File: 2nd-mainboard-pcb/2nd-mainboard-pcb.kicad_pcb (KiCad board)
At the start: 2 copper layers, 1 part, among them P1 USB_C_Plug_USB2.0

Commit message: managed libraries
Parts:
- added SW1: SW_DIP_x01, Button_Switch_SMD:SW_SPST_EVQQ2, F.Cu at (196.2, 59.4)
- added U1: ATmega328PB-A, Package_QFP:TQFP-32_7x7mm_P0.8mm, F.Cu at (131.1, 52.8)
- added U2: FT232RL, Package_SO:SSOP-28_5.3x10.2mm_P0.65mm, F.Cu at (120.0, 53.0)

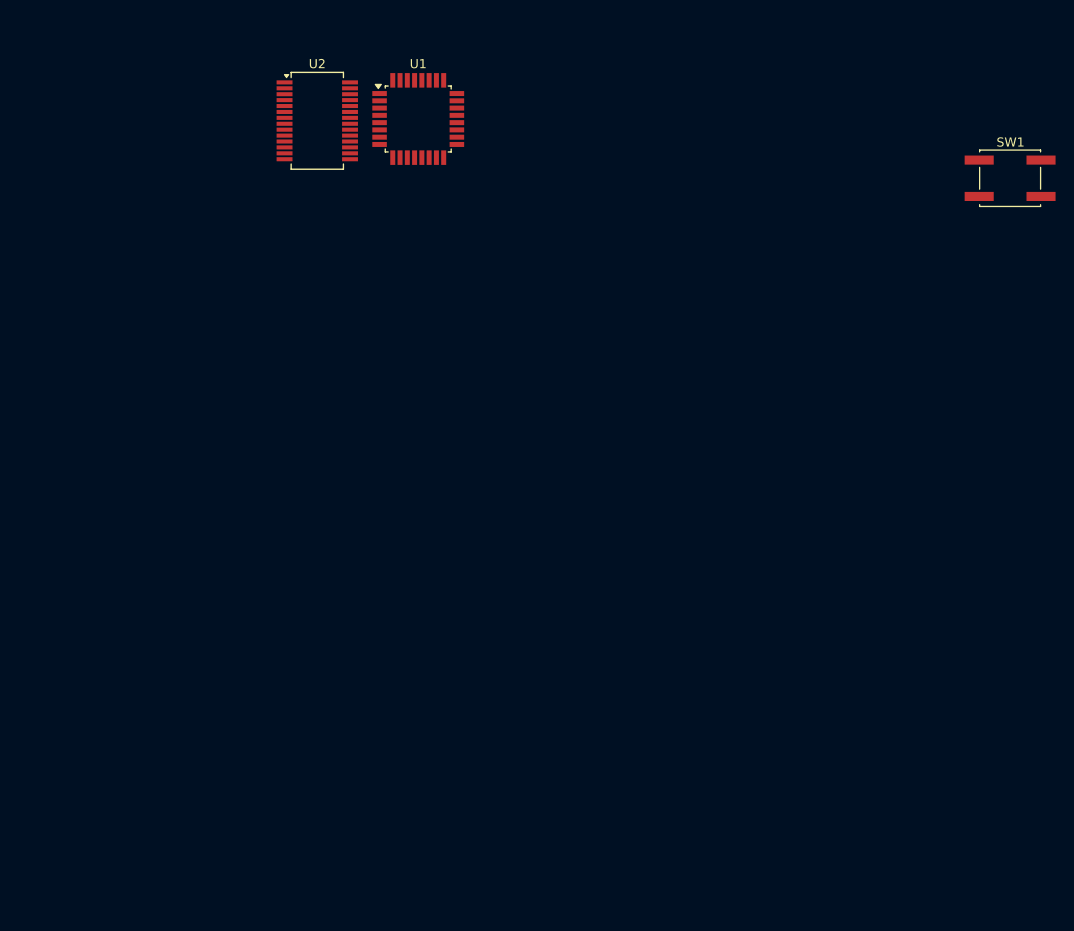
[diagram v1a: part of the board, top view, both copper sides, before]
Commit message: added test point and documentation
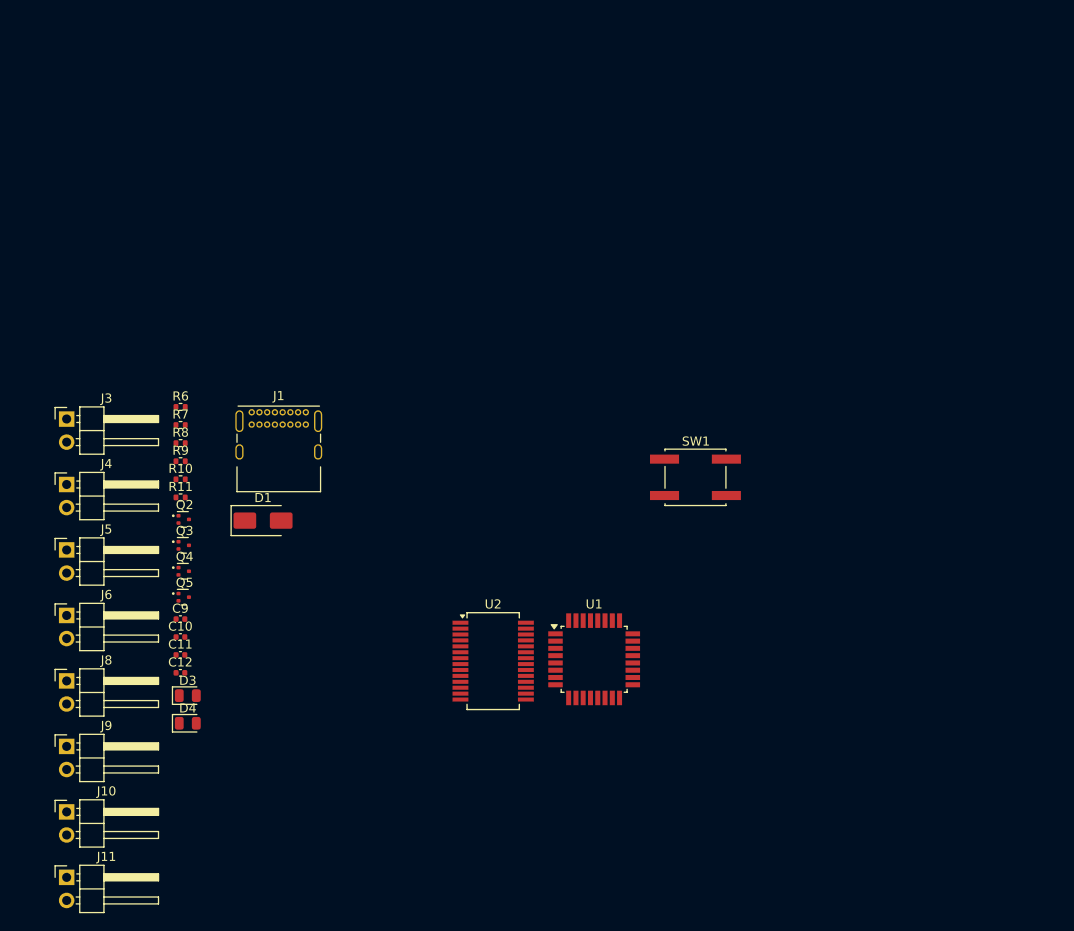
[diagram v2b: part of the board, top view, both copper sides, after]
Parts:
- added C10: 0.1µF, Capacitor_SMD:C_0402_1005Metric, F.Cu at (105.0, 109.8)
- added C11: 0.1µF, Capacitor_SMD:C_0402_1005Metric, F.Cu at (105.0, 111.8)
- added C12: 0.1µF, Capacitor_SMD:C_0402_1005Metric, F.Cu at (105.0, 113.8)
- added C9: 0.1µF, Capacitor_SMD:C_0402_1005Metric, F.Cu at (105.0, 107.8)
- added D1: SMAJ5.0A, Diode_SMD:D_SMA, F.Cu at (114.0, 97.0)
- added D3: YELLOW, LED_SMD:LED_0805_2012Metric, F.Cu at (105.8, 116.3)
- added D4: YELLOW, LED_SMD:LED_0805_2012Metric, F.Cu at (105.8, 119.3)
- added J1: USB_C_Receptacle, Connector_USB:USB_C_Receptacle_GCT_USB4085, F.Cu at (112.8, 85.1)
- added J10: FAN2, Connector_PinHeader_2.54mm:PinHeader_1x02_P2.54mm_Horizontal, F.Cu at (92.4, 129.0)
- added J11: FAN4, Connector_PinHeader_2.54mm:PinHeader_1x02_P2.54mm_Horizontal, F.Cu at (92.4, 136.2)
- added J3: T0, Connector_PinHeader_2.54mm:PinHeader_1x02_P2.54mm_Horizontal, F.Cu at (92.4, 85.8)
- added J4: T1, Connector_PinHeader_2.54mm:PinHeader_1x02_P2.54mm_Horizontal, F.Cu at (92.4, 93.0)
- added J5: T2, Connector_PinHeader_2.54mm:PinHeader_1x02_P2.54mm_Horizontal, F.Cu at (92.4, 100.2)
- added J6: T3, Connector_PinHeader_2.54mm:PinHeader_1x02_P2.54mm_Horizontal, F.Cu at (92.4, 107.4)
- added J8: FAN0, Connector_PinHeader_2.54mm:PinHeader_1x02_P2.54mm_Horizontal, F.Cu at (92.4, 114.6)
- added J9: FAN1, Connector_PinHeader_2.54mm:PinHeader_1x02_P2.54mm_Horizontal, F.Cu at (92.4, 121.8)
- added Q2: DTC143E, Package_TO_SOT_SMD:SOT-723, F.Cu at (105.3, 96.9)
- added Q3: DTC143E, Package_TO_SOT_SMD:SOT-723, F.Cu at (105.3, 99.7)
- added Q4: DTC143E, Package_TO_SOT_SMD:SOT-723, F.Cu at (105.3, 102.6)
- added Q5: DTC143E, Package_TO_SOT_SMD:SOT-723, F.Cu at (105.3, 105.4)
- added R10: 4k7, Resistor_SMD:R_0402_1005Metric, F.Cu at (105.0, 92.5)
- added R11: 330, Resistor_SMD:R_0402_1005Metric, F.Cu at (105.0, 94.5)
- added R6: 4k7, Resistor_SMD:R_0402_1005Metric, F.Cu at (105.0, 84.5)
- added R7: 4k7, Resistor_SMD:R_0402_1005Metric, F.Cu at (105.0, 86.5)
- added R8: 330, Resistor_SMD:R_0402_1005Metric, F.Cu at (105.0, 88.5)
- added R9: 4k7, Resistor_SMD:R_0402_1005Metric, F.Cu at (105.0, 90.5)
- moved U1 62.5 mm to (150.5, 112.3)
- moved U2 62.5 mm to (139.4, 112.5)
- moved SW1 47.7 mm to (161.6, 92.3)
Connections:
- SW1 pad 1: unconnected-(SW1-Pad1) -> GND
- SW1 pad 2: unconnected-(SW1-Pad2) -> reset
- U1 pad 12: unconnected-(U1-PB0-Pad12) -> FAN_0_PWM
- U1 pad 13: unconnected-(U1-PB1-Pad13) -> FAN_1_PWM
- U1 pad 14: unconnected-(U1-PB2-Pad14) -> FAN_2_PWM
- U1 pad 15: unconnected-(U1-PB3-Pad15) -> FAN_3_PWM
- U1 pad 16: unconnected-(U1-PB4-Pad16) -> LED_0
- U1 pad 17: unconnected-(U1-PB5-Pad17) -> LED_1
- U1 pad 18: unconnected-(U1-AVCC-Pad18) -> AREF
- U1 pad 20: unconnected-(U1-AREF-Pad20) -> AREF
- U1 pad 23: unconnected-(U1-PC0-Pad23) -> ADC0
- U1 pad 24: unconnected-(U1-PC1-Pad24) -> ADC1
- U1 pad 25: unconnected-(U1-PC2-Pad25) -> ADC2
- U1 pad 26: unconnected-(U1-PC3-Pad26) -> ADC3
- U1 pad 29: unconnected-(U1-~{RESET}/PC6-Pad29) -> reset
- U1 pad 30: unconnected-(U1-PD0-Pad30) -> RXD
- U1 pad 31: unconnected-(U1-PD1-Pad31) -> TXD
- U1 pad 4: +5V -> AREF
- U1 pad 7: unconnected-(U1-XTAL1/PB6-Pad7) -> Net-(U1-XTAL1/PB6)
- U1 pad 8: unconnected-(U1-XTAL2/PB7-Pad8) -> Net-(U1-XTAL2/PB7)
- U2 pad 1: unconnected-(U2-TXD-Pad1) -> TXD
- U2 pad 15: unconnected-(U2-USBD+-Pad15) -> USBD+
- U2 pad 16: unconnected-(U2-USBD--Pad16) -> USBD-
- U2 pad 19: unconnected-(U2-~{RESET}-Pad19) -> reset
- U2 pad 20: +5V -> AREF
- U2 pad 22: unconnected-(U2-CBUS1-Pad22) -> Net-(U2-CBUS1)
- U2 pad 23: unconnected-(U2-CBUS0-Pad23) -> Net-(U2-CBUS0)
- U2 pad 4: unconnected-(U2-VCCIO-Pad4) -> AREF
- U2 pad 5: unconnected-(U2-RXD-Pad5) -> RXD

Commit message: jtag funktionalität
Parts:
- removed P1: USB_C_Plug_USB2.0, Connector_USB:USB_C_Receptacle_GCT_USB4085
- added A1: Pololu_Breakout_DRV8825, Module:Pololu_Breakout-16_15.2x20.3mm, F.Cu at (218.7, 56.1)
- added C13: 0.1µF, Capacitor_SMD:CP_Elec_5x3, F.Cu at (187.9, 122.1)
- added C14: 0.22µF, Capacitor_SMD:C_0402_1005Metric, F.Cu at (184.9, 126.5)
- added C15: 0.22µF, Capacitor_SMD:C_0402_1005Metric, F.Cu at (184.9, 128.5)
- added C16: 0.1µF, Capacitor_SMD:C_0402_1005Metric, F.Cu at (184.9, 130.5)
- added C17: 0.1µF, Capacitor_SMD:C_0402_1005Metric, F.Cu at (184.9, 132.4)
- added C8: 0.1µF, Capacitor_SMD:CP_Elec_5x3, F.Cu at (187.9, 115.3)
- added D5: YELLOW, LED_SMD:LED_0805_2012Metric, F.Cu at (185.7, 137.0)
- added D6: YELLOW, LED_SMD:LED_0805_2012Metric, F.Cu at (185.7, 140.0)
- added D7: GREEN, LED_SMD:LED_0805_2012Metric, F.Cu at (257.3, 116.4)
- added J12: Fan_12/5V_Regelung, Connector_PinHeader_2.54mm:PinHeader_1x03_P2.54mm_Horizontal, F.Cu at (208.1, 77.5)
- added J7: Power, Connector_PinHeader_2.54mm:PinHeader_1x03_P2.54mm_Horizontal, F.Cu at (210.6, 107.5)
- added JP1: MEASO, Jumper:SolderJumper-2_P1.3mm_Bridged_Pad1.0x1.5mm, F.Cu at (188.5, 127.3)
- added JP2: MEASO, Jumper:SolderJumper-2_P1.3mm_Bridged_Pad1.0x1.5mm, F.Cu at (188.5, 130.9)
- added R12: 330, Resistor_SMD:R_0402_1005Metric, F.Cu at (189.3, 136.4)
- added R13: 330, Resistor_SMD:R_0402_1005Metric, F.Cu at (189.3, 138.4)
- added R17: 1k, Resistor_SMD:R_0402_1005Metric, F.Cu at (256.5, 119.0)
- added TP2: 5V_Test, TestPoint:TestPoint_Pad_D3.0mm, F.Cu at (252.5, 117.5)
- added TP3: GND_Test, TestPoint:TestPoint_Pad_D3.0mm, F.Cu at (252.5, 122.5)
- added TP4: 3V3_Test, TestPoint:TestPoint_Pad_D3.0mm, F.Cu at (252.5, 127.5)
- added TP5: 12V_Test, TestPoint:TestPoint_Pad_D3.0mm, F.Cu at (252.5, 132.6)
- moved J1 90.8 mm to (195.2, 123.1)
- moved D1 82.0 mm to (184.5, 55.0)
- moved U2 72.0 mm to (197.5, 70.0)
- moved U1 56.5 mm to (185.0, 67.5)
- moved SW1 51.8 mm to (200.0, 57.5)
- moved C11 45.5 mm to (67.5, 85.9)
- moved C12 45.5 mm to (67.5, 87.9)
- moved D3 45.5 mm to (68.3, 90.4)
- moved D4 45.5 mm to (68.3, 93.5)
- moved J10 45.5 mm to (55.0, 103.2)
- moved J6 45.5 mm to (55.0, 81.6)
- moved J8 45.5 mm to (55.0, 88.8)
- moved Q4 45.5 mm to (67.9, 76.7)
- moved R10 45.5 mm to (67.5, 66.6)
- moved R7 45.5 mm to (67.5, 60.7)
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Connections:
- net Net-(U1-XTAL1/PB6) renamed Quartz_2
- net Net-(U1-XTAL2/PB7) renamed Quartz_1
- J10 pad 2: AREF -> Fan_Versorgung
- J11 pad 2: AREF -> Fan_Versorgung
- J8 pad 2: AREF -> Fan_Versorgung
- J9 pad 2: AREF -> Fan_Versorgung

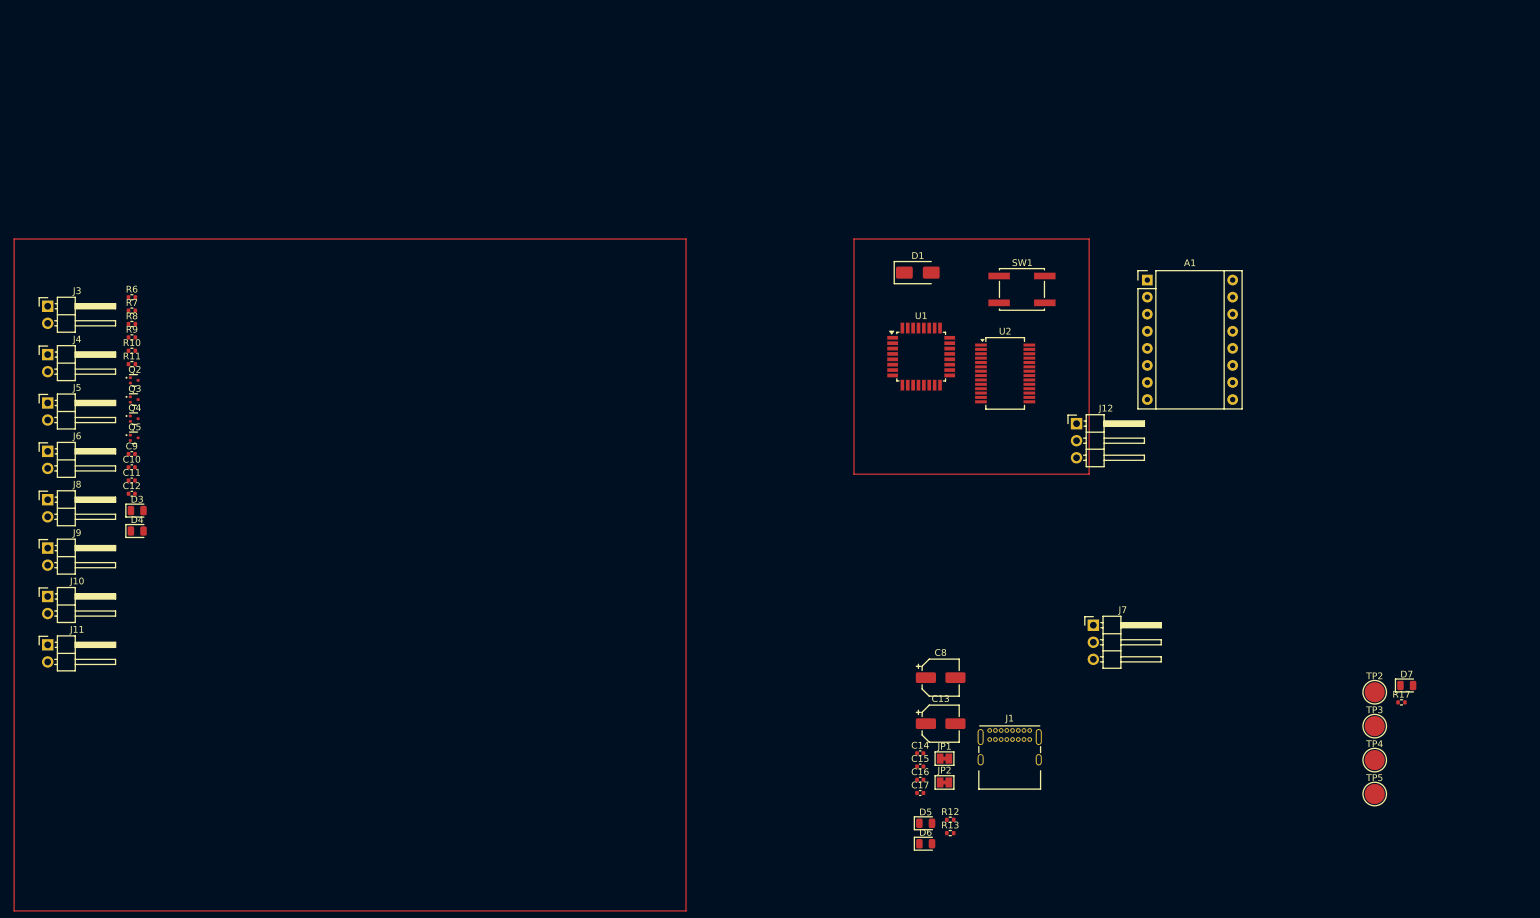
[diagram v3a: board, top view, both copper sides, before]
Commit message: added imported components, changed structure
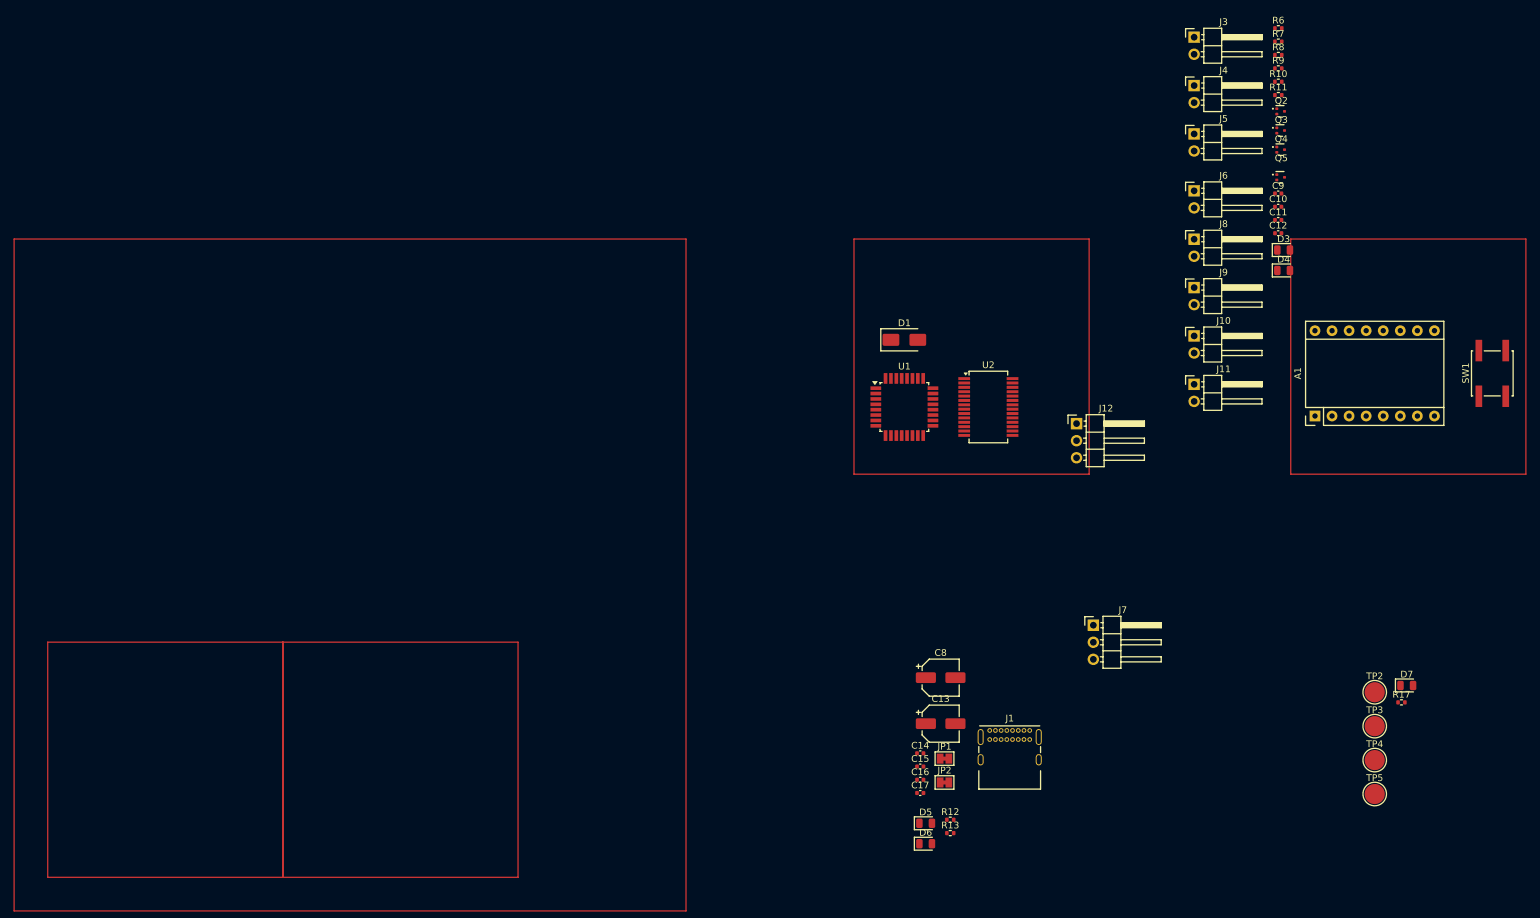
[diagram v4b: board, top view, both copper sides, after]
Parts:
- moved J3 175.3 mm to (225.6, 20.0)
- moved J4 175.3 mm to (225.6, 27.2)
- moved J5 175.3 mm to (225.6, 34.4)
- moved Q2 175.3 mm to (238.5, 31.0)
- moved Q3 175.3 mm to (238.5, 33.9)
- moved Q4 175.3 mm to (238.5, 36.7)
- moved R10 175.3 mm to (238.2, 26.6)
- moved R11 175.3 mm to (238.2, 28.6)
- moved R6 175.3 mm to (238.2, 18.6)
- moved R7 175.3 mm to (238.2, 20.6)
- moved R8 175.3 mm to (238.2, 22.6)
- moved R9 175.3 mm to (238.2, 24.6)
- moved C10 175.0 mm to (238.1, 45.2)
- moved C11 175.0 mm to (238.1, 47.2)
- moved C12 175.0 mm to (238.1, 49.1)
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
